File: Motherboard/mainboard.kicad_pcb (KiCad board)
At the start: 4 copper layers, 45.2 x 36 mm, 46 parts, among them IC1 BMX160, J1 Conn_01x01, J2 10118194-0001LF, J28 Conn_01x01, J29 Conn_01x01, J3 Micro_SD_Card, J30 Conn_01x01, J4 xf2m-2415-1a, J5 XF2M-1015-1A, J6 U.FL-R-SMT-1, J7 U.FL-R-SMT-1, SW1 KMR231NG LFS, U1 RFM95W-915S2, U2 ATSAMD51G_TQFN48, U3 DRV8848, U4 TPS82740BSIPR, U5 DRV8848, U6 MAX708RESA-T, U8 RFM95W-915S2

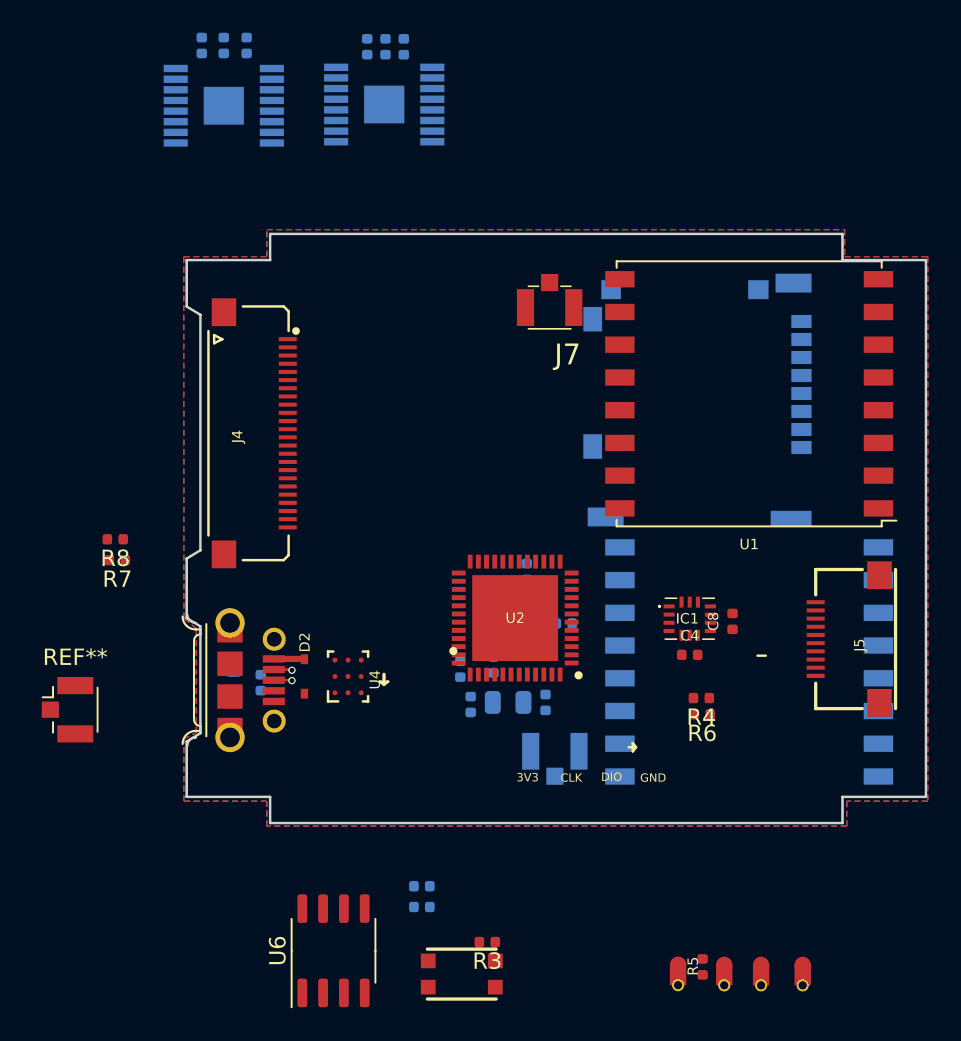
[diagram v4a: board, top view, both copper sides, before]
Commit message: updated pycubed board edge cuts, updated top layer copper edges, shifted USB card and flat flex connector (still need to shift camera connector)
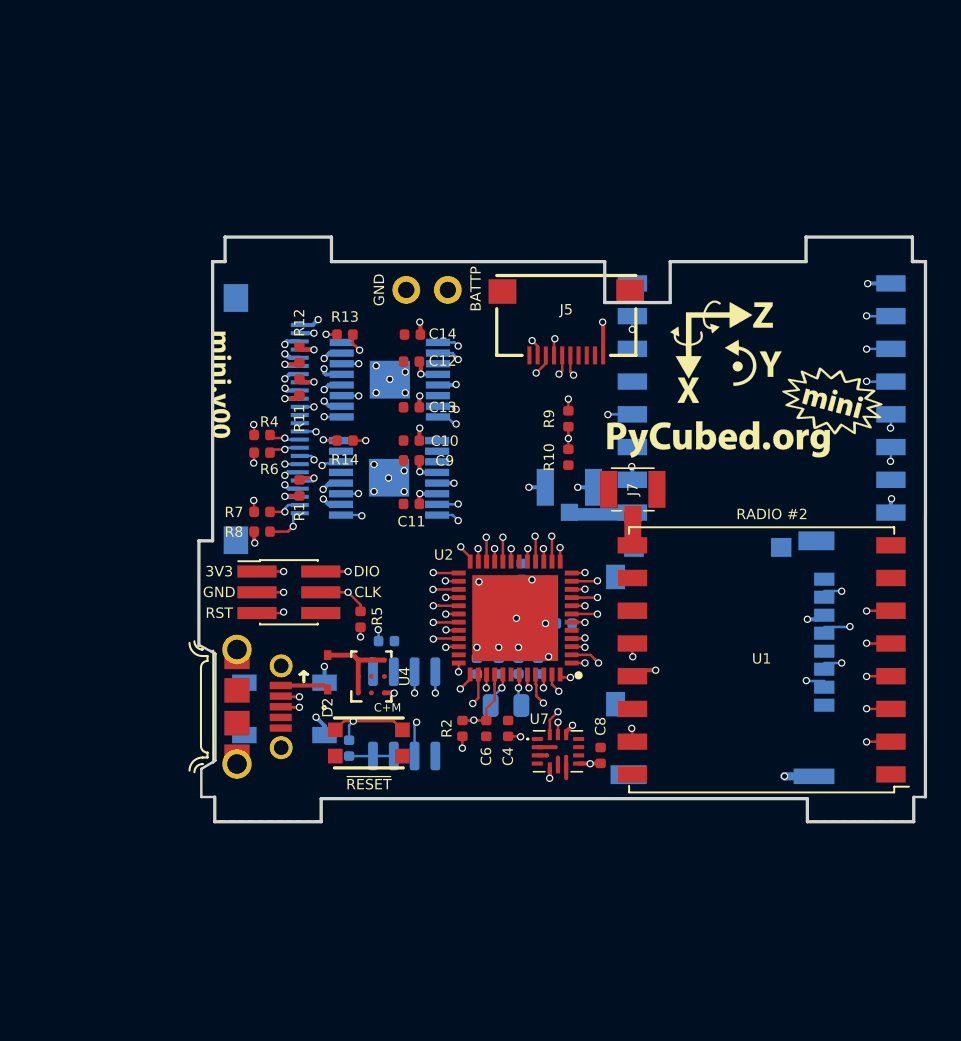
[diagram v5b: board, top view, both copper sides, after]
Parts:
- removed D1: GREEN, LED_SMD:LED_0603_1608Metric
- removed IC1: BMX160, custom-footprints:BMX160
- removed J28, J29, J30: Conn_01x01, custom-footprints:castellated_small_1side
- removed REF**: U.FL_Hirose_U.FL-R-SMT-1_Vertical, Connector_Coaxial:U.FL_Hirose_U.FL-R-SMT-1_Vertical
- added C16: 0.1uF, Capacitor_SMD:C_0402_1005Metric, B.Cu at (88.8, 98.4)
- added D3: WS2812B, LED_SMD:LED_WS2812B_PLCC4_5.0x5.0mm_P3.2mm, B.Cu at (82.6, 102.6)
- added FID1: Fiducial, custom-footprints:Fiducial_1mm_Silkscreen, F.Cu at (77.6, 76.1)
- added FID2: Fiducial, custom-footprints:Fiducial_1mm_Silkscreen, F.Cu at (77.6, 107.1)
- added FID3: Fiducial, custom-footprints:Fiducial_1mm_Silkscreen, F.Cu at (120.8, 76.1)
- added FID4: Fiducial, custom-footprints:Fiducial_1mm_Silkscreen, F.Cu at (115.8, 108.7)
- added J9: Conn_01x02, Connector_PinHeader_2.54mm:PinHeader_1x02_P2.54mm_Vertical, F.Cu at (90.0, 77.0)
- added R10: 100K, Resistor_SMD:R_0402_1005Metric, F.Cu at (99.9, 87.2)
- added R11: 0, Resistor_SMD:R_0402_1005Metric, F.Cu at (83.5, 82.9)
- added R12: 0, Resistor_SMD:R_0402_1005Metric, F.Cu at (83.5, 80.9)
- added R13: 100K, Resistor_SMD:R_0402_1005Metric, F.Cu at (86.3, 79.7)
- added R14: 10K, Resistor_SMD:R_0402_1005Metric, F.Cu at (86.3, 86.2)
- added R9: 100K, Resistor_SMD:R_0402_1005Metric, F.Cu at (99.9, 84.8)
- added Ref**: Val**, custom-footprints:XYZ_mini, F.Cu at (110.0, 81.3)
- added Ref**: Val**, custom-footprints:holliday, B.Cu at (76.3, 94.8)
- added Ref**: Val**, custom-footprints:version, B.Cu at (93.9, 105.6)
- added Ref**: Val**, custom-footprints:version, F.Cu at (78.7, 86.2)
- added Ref**: Val**, custom-footprints:pycubed_mini_logo, B.Cu at (97.5, 76.0)
- added Ref**: Val**, custom-footprints:pycubed_mini_logo, F.Cu at (117.5, 83.9)
- added U7: BMX160, custom-footprints:BMX160, F.Cu at (99.3, 105.2)
- C10, C11, C12, C13, C14, C6, C9, R2: moved to F.Cu
- J1: value Conn_01x01 -> Conn_01x06; footprint custom-footprints:castellated_small_1side -> Connector_PinHeader_1.27mm:PinHeader_2x03_P1.27mm_Vertical_SMD
- J4, R3, U6: moved to B.Cu
- R1: value 330 -> 0; moved to F.Cu
- moved J1 36.7 mm to (82.9, 95.4), turned to 0 degrees
- moved R4 31.3 mm to (81.2, 85.8)
- moved R6 31.3 mm to (81.2, 86.9)
- moved R5 29.8 mm to (87.2, 97.1), turned to 90 degrees
- moved C11 28.1 mm to (90.4, 90.0), turned to 0 degrees
- moved C9 25.3 mm to (90.4, 87.4), turned to 180 degrees
- moved U5 24.9 mm to (89.0, 88.4)
- moved C13 24.3 mm to (90.4, 84.1), turned to 0 degrees
- moved C10 24.1 mm to (90.4, 86.2), turned to 180 degrees
- moved J5 23.1 mm to (99.8, 81.0), turned to 180 degrees
- moved C12 22.5 mm to (90.4, 81.3), turned to 180 degrees
- moved C14 21.9 mm to (90.4, 79.7), turned to 180 degrees
- moved U3 16.8 mm to (89.0, 82.4), turned to 0 degrees
- moved U1 16.3 mm to (111.8, 99.6)
- moved J6 16.2 mm to (100.0, 89.0)
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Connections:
- C11 pad 2: 3V3 -> +3V3
- C13 pad 2: 3V3 -> +3V3
- J1 pad 1: /SWDIO -> +3V3
- J3 pad SH1: (no net) -> GND
- J4 pad 10: COIL3P -> SCL1
- J4 pad 11: BURN2 -> BATT_STATUS
- J4 pad 12: COIL3N -> +3V3
- J4 pad 13: Net-(J4-Pad13) -> +3V3
- J4 pad 14: Net-(J4-Pad14) -> GND
- J4 pad 15: SCL1 -> Net-(J4-Pad15)
- J4 pad 16: SDA1 -> COIL4_N
- J4 pad 18: Net-(J4-Pad18) -> COIL3_P
- J4 pad 20: Net-(J4-Pad20) -> COIL2_N
- J4 pad 21: GND -> Net-(J4-Pad21)
- J4 pad 22: 3V3 -> COIL1_P
- J4 pad 23: BATT_N -> GND
- J4 pad 3: COIL1P -> Net-(J4-Pad3)
- J4 pad 4: COIL1N -> COIL6_N
- J4 pad 6: COIL2P -> COIL5_P
- J4 pad 7: Net-(J4-Pad7) -> BURN1
- J4 pad 8: COIL2N -> BURN2
- J4 pad 9: BURN1 -> SDA1
- J5 pad 4: BATT_N -> GND
- J5 pad 5: EN_CAM -> MOSI
- J5 pad 6: CS_CAM -> SCK
- J5 pad 8: MOSI -> EN_CAM
- J5 pad 9: SCK -> CS_CAM
- R1 pad 1: Net-(D1-Pad1) -> Net-(J4-Pad3)
- R1 pad 2: /LED1 -> Net-(J4-Pad5)
- U1 pad 15: Net-(U1-Pad15) -> RF2_IO1
- U1 pad 5: CS_RF2 -> RF2_CS
- U2 pad 10: DAC1 -> BATTERY
- U2 pad 11: Net-(U2-Pad11) -> RF1_BUSY
- U2 pad 12: PA07 -> RF1_IO1
- U2 pad 16: Net-(U2-Pad16) -> EN_CAM
- U2 pad 19: RF_CS -> CS_CAM
- U2 pad 20: Net-(U2-Pad20) -> MINZ_1
- U2 pad 21: RF_RST -> MINZ_2
- U2 pad 22: RF_BUSY -> MINX_2
- U2 pad 23: RF_DIO3 -> MINX_1
- U2 pad 24: CS_CAM -> MINY_1
- U2 pad 27: CS_IMU -> BATT_STATUS
- U2 pad 28: Net-(U2-Pad28) -> M_EN
- U2 pad 29: EN_CAM -> BURN2
- U2 pad 3: DAC0 -> RF2_IO1
- U2 pad 30: PA21 -> M_FAULT
- U2 pad 31: PA22 -> BURN1
- U2 pad 32: PA23 -> MINY_2
- U2 pad 37: WDT_WDI -> Net-(D3-Pad4)
- U2 pad 38: RF_DIO2 -> WDT_WDI
- U2 pad 39: RF_DIO1 -> RF2_BUSY
- U2 pad 47: RF_DIO0 -> CS_SD
- U2 pad 48: /LED1 -> RF2_CS
- U2 pad 7: TX -> RF2_RST
- U2 pad 8: RX -> RF1_RST
- U2 pad 9: PA04 -> RF1_CS
- U3 pad 1: MXZ_EN -> M_EN
- U3 pad 11: 3V3 -> +3V3
- U3 pad 14: 3V3 -> +3V3
- U3 pad 2: MOX_1 -> COIL4_N
- U3 pad 4: MOX_2 -> COIL3_P
- U3 pad 5: MOZ_2 -> COIL2_N
- U3 pad 7: MOZ_1 -> COIL1_P
- U3 pad 8: DXZ_FAULT -> M_FAULT
- U5 pad 1: MXZ_EN -> M_EN
- U5 pad 10: MINZ_2 -> Net-(U5-Pad10)
- U5 pad 11: 3V3 -> +3V3
- U5 pad 14: 3V3 -> +3V3
- U5 pad 15: MINX_2 -> MINY_2
- U5 pad 16: MINX_1 -> MINY_1
- U5 pad 2: MINX_1 -> COIL6_N
- U5 pad 4: MINX_2 -> COIL5_P
- U5 pad 5: MOZ_2 -> Net-(U5-Pad5)
- U5 pad 7: MOZ_1 -> Net-(U5-Pad7)
- U5 pad 8: DXZ_FAULT -> M_FAULT2
- U5 pad 9: MINZ_1 -> Net-(U5-Pad9)
- U8 pad 11: RF_DIO3 -> Net-(U8-Pad11)
- U8 pad 12: RF_BUSY -> RF1_BUSY
- U8 pad 14: RF_DIO0 -> Net-(U8-Pad14)
- U8 pad 15: RF_DIO1 -> RF1_IO1
- U8 pad 16: RF_DIO2 -> Net-(U8-Pad16)
- U8 pad 5: CS_RF1 -> RF1_CS
- U8 pad 6: RF_RST -> RF1_RST
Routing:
- net MISO: track 0.00 -> 66.5 mm, vias 0 -> 5
- net MOSI: track 0.00 -> 58.9 mm, vias 0 -> 5
- net SCK: track 0.00 -> 55.5 mm, vias 0 -> 5
- net BATT_P: track 0.00 -> 44.9 mm, vias 0 -> 7
- net SCL1: track 0.00 -> 34.9 mm, vias 0 -> 3
- net SDA1: track 0.00 -> 32.6 mm, vias 0 -> 3
- net GND: track 0.00 -> 29.9 mm, vias 0 -> 38
- net ~RESET: track 0.00 -> 29.9 mm, vias 0 -> 3
- net RF1_CS: track 0.00 -> 24.6 mm, vias 0 -> 2
- net RF1_RST: track 0.00 -> 24.0 mm, vias 0 -> 2
- net M_FAULT: track 0.00 -> 23.6 mm, vias 0 -> 3
- net RF2_CS: track 0.00 -> 21.3 mm, vias 0 -> 2
- net /SWCLK: track 0.00 -> 20.3 mm, vias 0 -> 2
- net RF2_RST: track 0.00 -> 19.6 mm, vias 0 -> 2
- net +3V3: track 0.00 -> 18.5 mm, vias 0 -> 21
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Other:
- board size 45.2 x 36 mm -> 44.4 x 35.7 mm
- board text added: "BATTP"
- board text added: "C+M"
- board text added: "RADIO #1"
- board text added: "RADIO #2"
- board text added: "RST"
- board text added: "~RESET"
